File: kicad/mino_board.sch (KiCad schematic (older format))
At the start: 40 parts, among them J1-2 Conn_01x04, J10 Conn_01x04, J2 Conn_01x05, J4 Conn_02x10_Counter_Clockwise, P1 LED, P2 LED, P3 LED, P4 LED, X1 SW_Push, Y1 SW_Push

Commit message: More footprints again
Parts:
- added JEXTRAS: Conn_01x05, symbol Connector_Generic:Conn_01x05
- added JPS5JUMPER: Conn_01x02, symbol Connector_Generic:Conn_01x02
- added SW_THUMBR: SW_SPDT, symbol Switch:SW_SPDT
- renumbered SW_THUMBS to SW_THUMBL
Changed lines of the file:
@@
 $EndComp
 $Comp
-L Switch:SW_SPDT SW_THUMBS
+L Switch:SW_SPDT SW_THUMBL
 U 1 1 61698E4A
 P 5550 950
-F 0 "SW_THUMBS" H 5550 1235 50  0000 C CNN
+F 0 "SW_THUMBL" H 5550 1235 50  0000 C CNN
 F 1 "SW_SPDT" H 5550 1144 50  0000 C CNN
 F 2 "" H 5550 950 50  0001 C CNN
@@
 	1    0    0    -1
 $EndComp
+$Comp
+L Switch:SW_SPDT SW_THUMBR
+U 1 1 6169939A
+P 5550 1650
+F 0 "SW_THUMBR" H 5550 1935 50  0000 C CNN
+F 1 "SW_SPDT" H 5550 1844 50  0000 C CNN
+F 2 "" H 5550 1650 50  0001 C CNN
+F 3 "~" H 5550 1650 50  0001 C CNN
+	1    5550 1650
+	1    0    0    -1
+$EndComp
+$Comp
+L Connector_Generic:Conn_01x05 JEXTRAS
+U 1 1 616AC5C6
+P 9650 1250
+F 0 "JEXTRAS" H 9730 1292 50  0000 L CNN
+F 1 "Conn_01x05" H 9730 1201 50  0000 L CNN
+F 2 "" H 9650 1250 50  0001 C CNN
+F 3 "~" H 9650 1250 50  0001 C CNN
+	1    9650 1250
+	1    0    0    -1
+$EndComp
+$Comp
+L Connector_Generic:Conn_01x02 JPS5JUMPER
+U 1 1 616B1ABF
+P 9450 2300
+F 0 "JPS5JUMPER" H 9530 2292 50  0000 L CNN
+F 1 "Conn_01x02" H 9530 2201 50  0000 L CNN
+F 2 "" H 9450 2300 50  0001 C CNN
+F 3 "~" H 9450 2300 50  0001 C CNN
+	1    9450 2300
+	1    0    0    -1
+$EndComp

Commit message: WIring and changes
Wire everything except audio, remove the PS5 board bits temporarily until I become more familiar with how it works.
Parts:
- removed JEXTRAS: Conn_01x05, symbol Connector_Generic:Conn_01x05
- removed JPS51: Conn_01x06, symbol Connector_Generic:Conn_01x06
- removed JPS52, JPS5JUMPER: Conn_01x02, symbol Connector_Generic:Conn_01x02
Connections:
- net at J4.3 (Pin_3), RIGHT1.1: now also SW_THUMBR.1 (A); no longer RIGHT2.1
- net at J4.4 (Pin_4), LEFT1.1: now also SW_THUMBL.1 (A); no longer LEFT2.1
- net at J10.2 (Pin_2), L3.1: now also SW_THUMBL.3 (C)
- net at J10.3 (Pin_3), R3.1: now also SW_THUMBR.3 (C)
- net at SW_SOCD.1 (A): now also JSOCD.1 (Pin_1)
- net at SW_SOCD.2 (B): now also JSOCD.2 (Pin_2)
- net at SW_THUMBL.2 (B): now also LEFT2.1
- net at SW_THUMBR.2 (B): now also RIGHT2.1
- net at SW_STICK.1: now also JSTICKTYPE.1 (Pin_1)
- net at SW_STICK.2: now also JSTICKTYPE.3 (Pin_3)
- net at SW_STICK.3: now also JSTICKTYPE.2 (Pin_2)
- net at SW_STICK.4: now also JSTICKTYPE.4 (Pin_4)
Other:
- moved on the sheet: JAUDIO, JSOCD, JSTICKTYPE, SW_THUMBL, SW_THUMBR
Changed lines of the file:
@@
 	4300 7600 5550 7600
 Wire Wire Line
-	5550 7600 5550 4850
-Wire Wire Line
-	5550 4850 5650 4850
-Wire Wire Line
-	5550 4850 5550 4350
-Wire Wire Line
 	5550 4350 5650 4350
-Connection ~ 5550 4850
 Wire Wire Line
 	3850 5350 4100 5350
@@
 	4100 7400 1750 7400
 Wire Wire Line
-	1750 7400 1750 6400
-Wire Wire Line
-	1750 6400 1950 6400
-Wire Wire Line
-	1750 6400 1750 5950
-Wire Wire Line
 	1750 5950 1950 5950
-Connection ~ 1750 6400
 Wire Wire Line
 	3850 5250 4400 5250
@@
 	9700 5800 7450 5800
 Wire Wire Line
-	7450 5800 7450 5950
+	7450 5800 7450 5900
 Wire Wire Line
 	9700 5900 8100 5900
 Wire Wire Line
-	8100 5900 8100 5600
+	8100 5900 8100 5650
 $Comp
 L Switch:SW_SPDT SW_SOCD
@@
 $EndComp
 $Comp
-L Switch:SW_SPDT SW_THUMBL
-U 1 1 61698E4A
-P 5550 950
-F 0 "SW_THUMBL" H 5550 1235 50  0000 C CNN
-F 1 "SW_SPDT" H 5550 1144 50  0000 C CNN
-F 2 "" H 5550 950 50  0001 C CNN
-F 3 "~" H 5550 950 50  0001 C CNN
-	1    5550 950
-	1    0    0    -1
-$EndComp
-$Comp
 L Switch:SW_SP3T SW_STICK
 U 1 1 6169A4AE
@@
 L Connector_Generic:Conn_01x04 JSTICKTYPE
 U 1 1 616A468F
-P 7700 2350
-F 0 "JSTICKTYPE" H 7780 2342 50  0000 L CNN
-F 1 "Conn_01x04" H 7780 2251 50  0000 L CNN
-F 2 "" H 7700 2350 50  0001 C CNN
-F 3 "~" H 7700 2350 50  0001 C CNN
-	1    7700 2350
-	1    0    0    -1
-$EndComp
-$Comp
-L Connector_Generic:Conn_01x02 JPS52
-U 1 1 616A5060
-P 7650 3000
-F 0 "JPS52" H 7730 2992 50  0000 L CNN
-F 1 "Conn_01x02" H 7730 2901 50  0000 L CNN
-F 2 "" H 7650 3000 50  0001 C CNN
-F 3 "~" H 7650 3000 50  0001 C CNN
-	1    7650 3000
+P 6900 1550
+F 0 "JSTICKTYPE" H 6980 1542 50  0000 L CNN
+F 1 "Conn_01x04" H 6980 1451 50  0000 L CNN
+F 2 "" H 6900 1550 50  0001 C CNN
+F 3 "~" H 6900 1550 50  0001 C CNN
+	1    6900 1550
 	1    0    0    -1
 $EndComp
@@
 L Connector_Generic:Conn_01x02 JSOCD
 U 1 1 616A5F1B
-P 7650 3450
-F 0 "JSOCD" H 7730 3442 50  0000 L CNN
-F 1 "Conn_01x02" H 7730 3351 50  0000 L CNN
-F 2 "" H 7650 3450 50  0001 C CNN
-F 3 "~" H 7650 3450 50  0001 C CNN
-	1    7650 3450
-	1    0    0    -1
-$EndComp
-$Comp
-L Connector_Generic:Conn_01x06 JPS51
-U 1 1 616A6B41
-P 9000 3200
-F 0 "JPS51" H 9080 3192 50  0000 L CNN
-F 1 "Conn_01x06" H 9080 3101 50  0000 L CNN
-F 2 "" H 9000 3200 50  0001 C CNN
-F 3 "~" H 9000 3200 50  0001 C CNN
-	1    9000 3200
+P 5050 950
+F 0 "JSOCD" H 5130 942 50  0000 L CNN
+F 1 "Conn_01x02" H 5130 851 50  0000 L CNN
+F 2 "" H 5050 950 50  0001 C CNN
+F 3 "~" H 5050 950 50  0001 C CNN
+	1    5050 950
 	1    0    0    -1
 $EndComp
@@
 L Connector_Generic:Conn_01x06 JAUDIO
 U 1 1 616A715C
-P 9000 4000
-F 0 "JAUDIO" H 9080 3992 50  0000 L CNN
-F 1 "Conn_01x06" H 9080 3901 50  0000 L CNN
-F 2 "" H 9000 4000 50  0001 C CNN
-F 3 "~" H 9000 4000 50  0001 C CNN
-	1    9000 4000
+P 8800 1200
+F 0 "JAUDIO" H 8880 1192 50  0000 L CNN
+F 1 "Conn_01x06" H 8880 1101 50  0000 L CNN
+F 2 "" H 8800 1200 50  0001 C CNN
+F 3 "~" H 8800 1200 50  0001 C CNN
+	1    8800 1200
 	1    0    0    -1
 $EndComp
@@
 L Switch:SW_SPDT SW_THUMBR
 U 1 1 6169939A
-P 5550 1650
-F 0 "SW_THUMBR" H 5550 1935 50  0000 C CNN
-F 1 "SW_SPDT" H 5550 1844 50  0000 C CNN
-F 2 "" H 5550 1650 50  0001 C CNN
-F 3 "~" H 5550 1650 50  0001 C CNN
-	1    5550 1650
-	1    0    0    -1
-$EndComp
-$Comp
-L Connector_Generic:Conn_01x05 JEXTRAS
-U 1 1 616AC5C6
-P 9650 1250
-F 0 "JEXTRAS" H 9730 1292 50  0000 L CNN
-F 1 "Conn_01x05" H 9730 1201 50  0000 L CNN
-F 2 "" H 9650 1250 50  0001 C CNN
-F 3 "~" H 9650 1250 50  0001 C CNN
-	1    9650 1250
-	1    0    0    -1
-$EndComp
-$Comp
-L Connector_Generic:Conn_01x02 JPS5JUMPER
-U 1 1 616B1ABF
-P 9450 2300
-F 0 "JPS5JUMPER" H 9530 2292 50  0000 L CNN
-F 1 "Conn_01x02" H 9530 2201 50  0000 L CNN
-F 2 "" H 9450 2300 50  0001 C CNN
-F 3 "~" H 9450 2300 50  0001 C CNN
-	1    9450 2300
-	1    0    0    -1
-$EndComp
+P 6150 7150
+F 0 "SW_THUMBR" H 6150 7435 50  0000 C CNN
+F 1 "SW_SPDT" H 6150 7344 50  0000 C CNN
+F 2 "" H 6150 7150 50  0001 C CNN
+F 3 "~" H 6150 7150 50  0001 C CNN
+	1    6150 7150
+	-1   0    0    1
+$EndComp
+Wire Wire Line
+	5550 4350 5550 7250
+Wire Wire Line
+	1750 5950 1750 6950
+$Comp
+L Switch:SW_SPDT SW_THUMBL
+U 1 1 61698E4A
+P 1300 6400
+F 0 "SW_THUMBL" H 1300 6685 50  0000 C CNN
+F 1 "SW_SPDT" H 1300 6594 50  0000 C CNN
+F 2 "" H 1300 6400 50  0001 C CNN
+F 3 "~" H 1300 6400 50  0001 C CNN
+	1    1300 6400
+	-1   0    0    1
+$EndComp
+Wire Wire Line
+	5550 7250 5950 7250
+Connection ~ 5550 7250
+Wire Wire Line
+	5550 7250 5550 7600
+Wire Wire Line
+	6350 7150 6350 6450
+Wire Wire Line
+	6350 6450 5400 6450
+Wire Wire Line
+	5400 6450 5400 4850
+Wire Wire Line
+	5400 4850 5650 4850
+Wire Wire Line
+	1500 6400 1950 6400
+Wire Wire Line
+	1750 6950 800  6950
+Wire Wire Line
+	800  6950 800  6500
+Wire Wire Line
+	800  6500 1100 6500
+Connection ~ 1750 6950
+Wire Wire Line
+	1750 6950 1750 7400
+Wire Wire Line
+	7450 5900 6500 5900
+Wire Wire Line
+	6500 5900 6500 7750
+Wire Wire Line
+	6500 7750 550  7750
+Wire Wire Line
+	550  7750 550  6300
+Wire Wire Line
+	550  6300 1100 6300
+Connection ~ 7450 5900
+Wire Wire Line
+	7450 5900 7450 5950
+Wire Wire Line
+	8100 5650 6150 5650
+Wire Wire Line
+	6150 5650 6150 6900
+Wire Wire Line
+	6150 6900 5800 6900
+Wire Wire Line
+	5800 6900 5800 7050
+Wire Wire Line
+	5800 7050 5950 7050
+Connection ~ 8100 5650
+Wire Wire Line
+	8100 5650 8100 5600
+Wire Wire Line
+	4850 950  4850 850
+Wire Wire Line
+	4850 850  4650 850
+Wire Wire Line
+	4850 1050 4850 1300
+Wire Wire Line
+	4850 1300 3900 1300
+Wire Wire Line
+	3900 1300 3900 950
+Wire Wire Line
+	3900 950  4250 950
+Wire Wire Line
+	6700 1550 6500 1550
+Wire Wire Line
+	6500 1550 6500 950
+Wire Wire Line
+	6900 950  7300 950
+Wire Wire Line
+	7300 950  7300 2100
+Wire Wire Line
+	7300 2100 6400 2100
+Wire Wire Line
+	6400 2100 6400 1650
+Wire Wire Line
+	6400 1650 6700 1650
+Wire Wire Line
+	6900 850  7100 850
+Wire Wire Line
+	7100 850  7100 1200
+Wire Wire Line
+	7100 1200 6600 1200
+Wire Wire Line
+	6600 1200 6600 1450
+Wire Wire Line
+	6600 1450 6700 1450
+Wire Wire Line
+	6900 1050 7500 1050
+Wire Wire Line
+	7500 1050 7500 1950
+Wire Wire Line
+	7500 1950 6700 1950
+Wire Wire Line
+	6700 1950 6700 1750
 $EndSCHEMATC

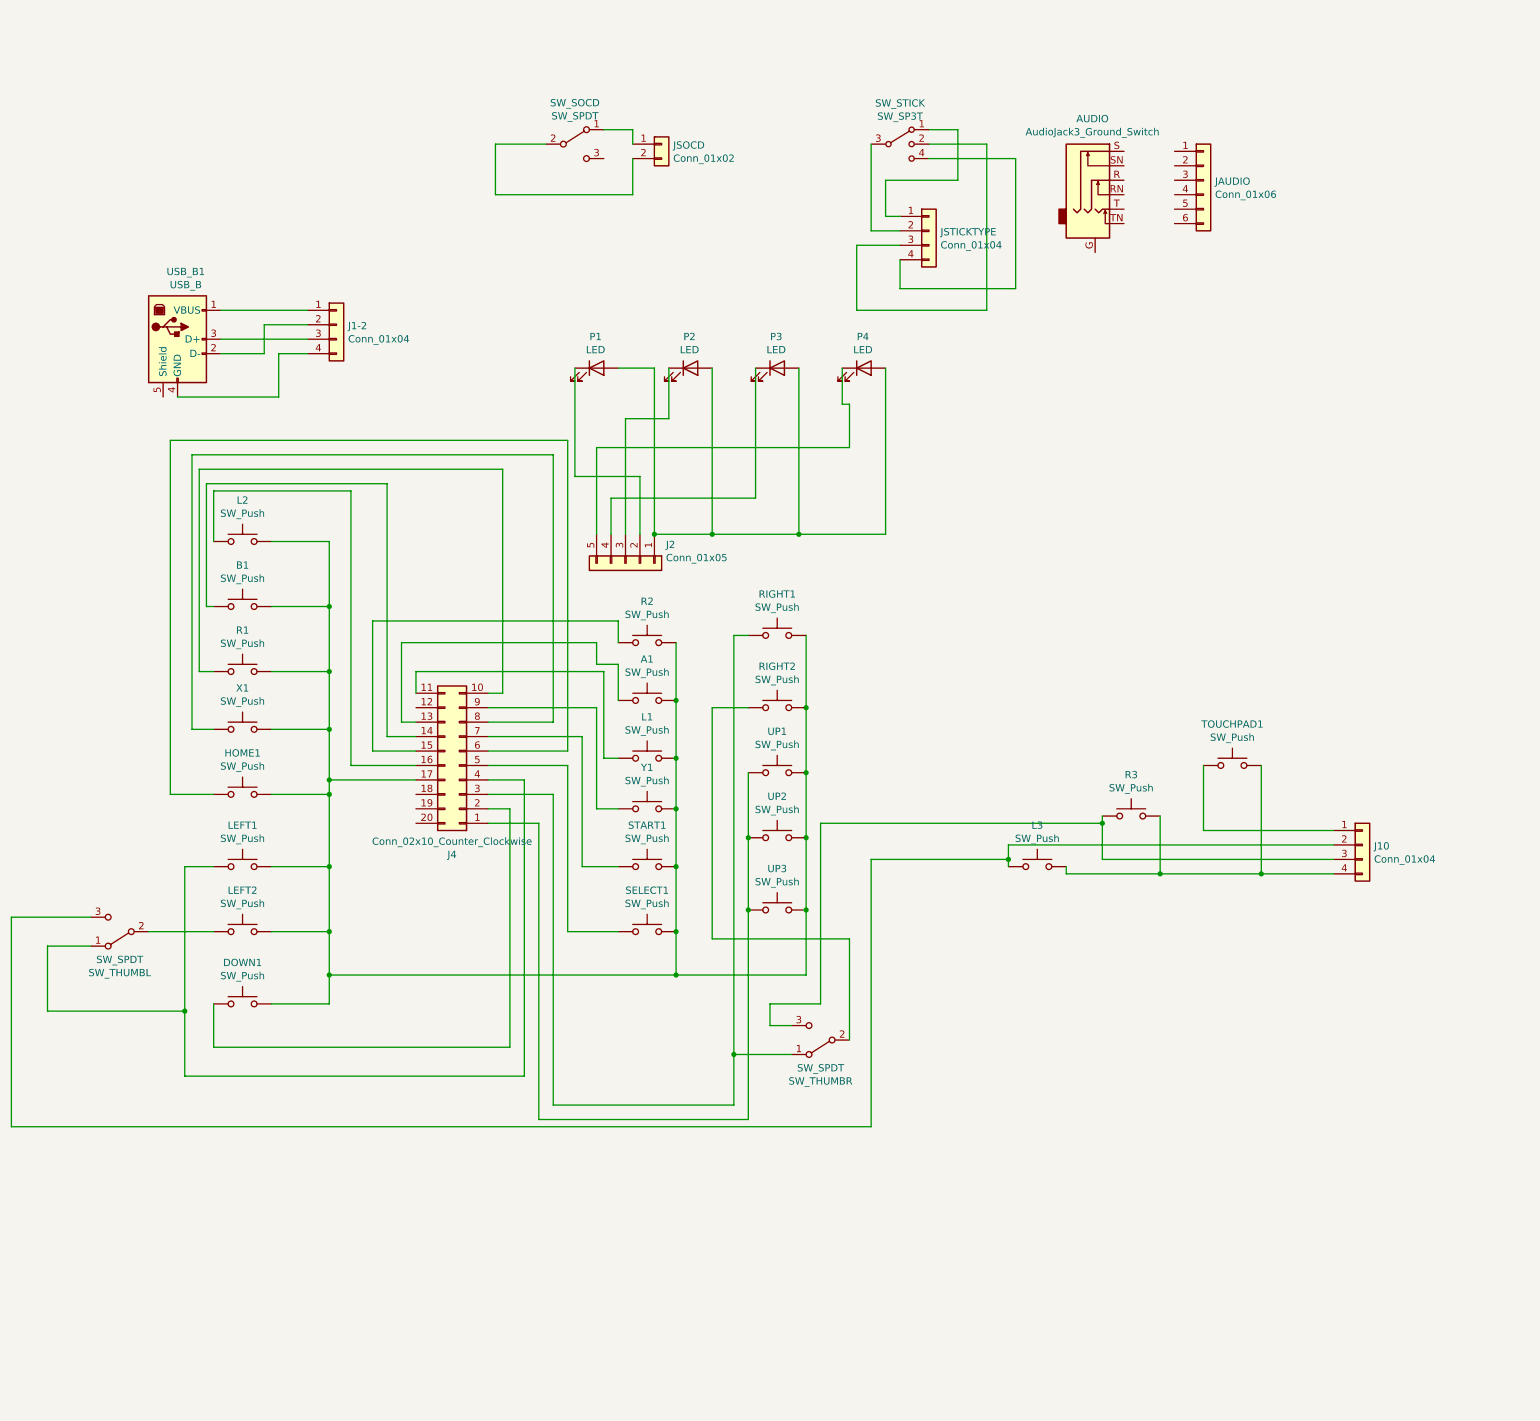
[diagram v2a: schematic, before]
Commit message: Dip Switches
Swap out the toggle switches for dip switches to control the spare thumb buttons.
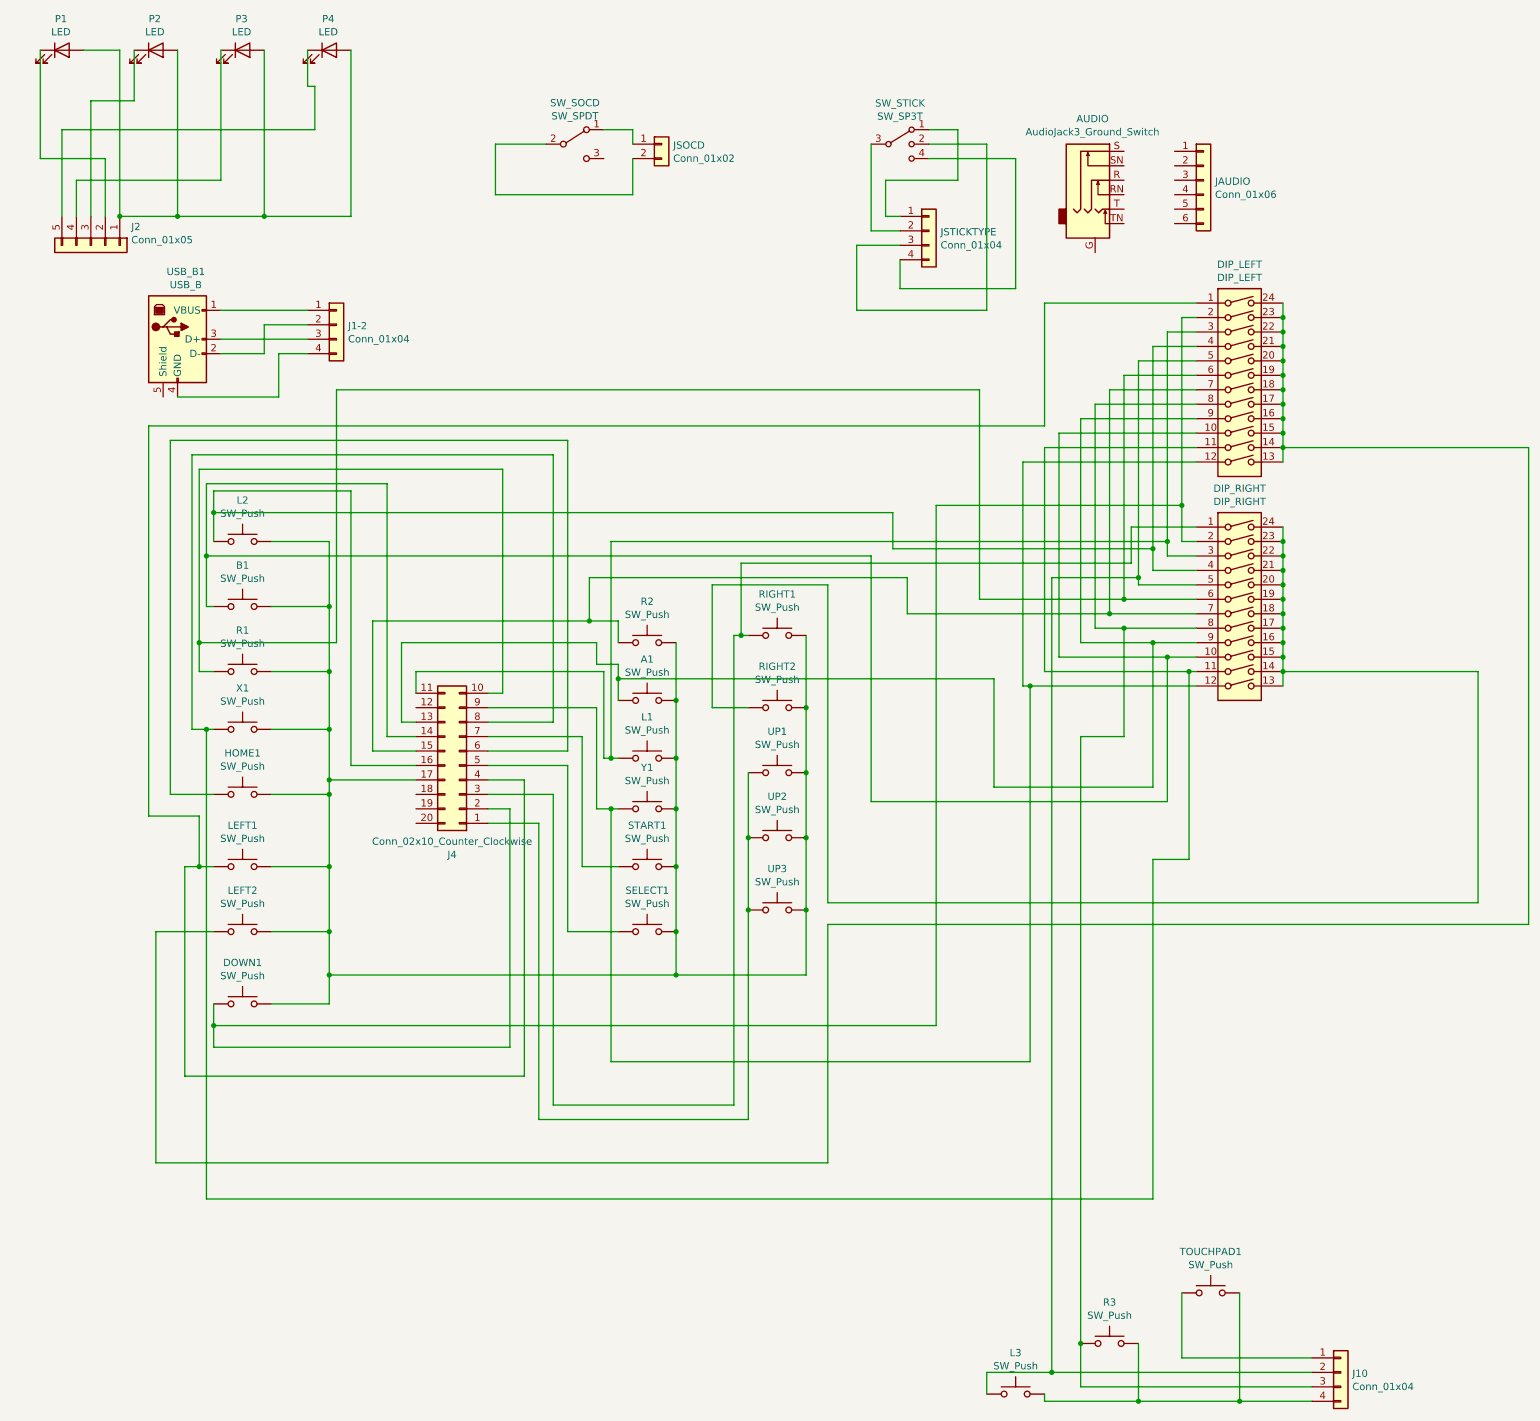
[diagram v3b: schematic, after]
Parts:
- removed SW_THUMBL, SW_THUMBR: SW_SPDT, symbol Switch:SW_SPDT
- added DIP_LEFT: DIP_LEFT, symbol Switch:SW_DIP_x12
- added DIP_RIGHT: DIP_RIGHT, symbol Switch:SW_DIP_x12
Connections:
- net at J4.10 (Pin_10), R1.1: now also DIP_LEFT.6, DIP_RIGHT.6
- net at J4.11 (Pin_11), L1.1: now also DIP_LEFT.3, DIP_RIGHT.3
- net at A1.1, J4.13 (Pin_13): now also DIP_LEFT.9, DIP_RIGHT.9
- net at B1.1, J4.14 (Pin_14): now also DIP_LEFT.10, DIP_RIGHT.10
- net at J4.15 (Pin_15), R2.1: now also DIP_LEFT.7, DIP_RIGHT.7
- net at J4.16 (Pin_16), L2.1: now also DIP_LEFT.4, DIP_RIGHT.4
- net at DOWN1.1, J4.2 (Pin_2): now also DIP_LEFT.2, DIP_RIGHT.2
- net at J4.3 (Pin_3), RIGHT1.1: now also DIP_RIGHT.1
- net at J4.4 (Pin_4), LEFT1.1: now also DIP_LEFT.1
- net at J4.8 (Pin_8), X1.1: now also DIP_LEFT.11, DIP_RIGHT.11
- net at J4.9 (Pin_9), Y1.1: now also DIP_LEFT.12, DIP_RIGHT.12
- net at J10.2 (Pin_2), L3.1: now also DIP_LEFT.5, DIP_RIGHT.5
- net at J10.3 (Pin_3), R3.1: now also DIP_LEFT.8, DIP_RIGHT.8
- net at RIGHT2.1: now also DIP_RIGHT.13, DIP_RIGHT.14, DIP_RIGHT.15, DIP_RIGHT.16, DIP_RIGHT.17, DIP_RIGHT.18, DIP_RIGHT.19, DIP_RIGHT.20, DIP_RIGHT.21, DIP_RIGHT.22, DIP_RIGHT.23, DIP_RIGHT.24
- net at LEFT2.1: now also DIP_LEFT.13, DIP_LEFT.14, DIP_LEFT.15, DIP_LEFT.16, DIP_LEFT.17, DIP_LEFT.18, DIP_LEFT.19, DIP_LEFT.20, DIP_LEFT.21, DIP_LEFT.22, DIP_LEFT.23, DIP_LEFT.24
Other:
- moved on the sheet: J10, J2, L3, P1, P2, P3, P4, R3, TOUCHPAD1

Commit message: Remove Audio Jack
Remove the audio jack until I can figure out how it works
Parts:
- removed AUDIO: AudioJack3_Ground_Switch, symbol Connector:AudioJack3_Ground_Switch
- removed JAUDIO: Conn_01x06, symbol Connector_Generic:Conn_01x06
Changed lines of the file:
@@
-$EndComp
-$Comp
-L Connector:AudioJack3_Ground_Switch AUDIO
-U 1 1 616A2FE6
-P 8050 1200
-F 0 "AUDIO" H 8032 1625 50  0000 C CNN
-F 1 "AudioJack3_Ground_Switch" H 8032 1534 50  0000 C CNN
-F 2 "" H 8050 1200 50  0001 C CNN
-F 3 "~" H 8050 1200 50  0001 C CNN
-	1    8050 1200
-	1    0    0    -1
 $EndComp
 $Comp
@@
 	1    0    0    -1
 $EndComp
-$Comp
-L Connector_Generic:Conn_01x06 JAUDIO
-U 1 1 616A715C
-P 8800 1200
-F 0 "JAUDIO" H 8880 1192 50  0000 L CNN
-F 1 "Conn_01x06" H 8880 1101 50  0000 L CNN
-F 2 "" H 8800 1200 50  0001 C CNN
-F 3 "~" H 8800 1200 50  0001 C CNN
-	1    8800 1200
-	1    0    0    -1
-$EndComp

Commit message: Route the new board
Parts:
- renumbered DIP_LEFT to DIP_LEFT1, DIP_RIGHT to DIP_RIGHT1, JSOCD to JSOCD1, JSTICKTYPE to JSTICKTYPE1, SW_SOCD to SW_SOCD1, SW_STICK to SW_STICK1
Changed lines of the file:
@@
 	9550 9550 7950 9550
 $Comp
-L Switch:SW_SPDT SW_SOCD
+L Switch:SW_SPDT SW_SOCD1
 U 1 1 61698368
 P 4450 950
-F 0 "SW_SOCD" H 4450 1235 50  0000 C CNN
+F 0 "SW_SOCD1" H 4450 1235 50  0000 C CNN
 F 1 "SW_SPDT" H 4450 1144 50  0000 C CNN
 F 2 "" H 4450 950 50  0001 C CNN
@@
 $EndComp
 $Comp
-L Switch:SW_SP3T SW_STICK
+L Switch:SW_SP3T SW_STICK1
 U 1 1 6169A4AE
 P 6700 950
-F 0 "SW_STICK" H 6700 1233 50  0000 C CNN
+F 0 "SW_STICK1" H 6700 1233 50  0000 C CNN
 F 1 "SW_SP3T" H 6700 1142 50  0000 C CNN
 F 2 "" H 6075 1125 50  0001 C CNN
@@
 $EndComp
 $Comp
-L Connector_Generic:Conn_01x04 JSTICKTYPE
+L Connector_Generic:Conn_01x04 JSTICKTYPE1
 U 1 1 616A468F
 P 6900 1550
-F 0 "JSTICKTYPE" H 6980 1542 50  0000 L CNN
+F 0 "JSTICKTYPE1" H 6980 1542 50  0000 L CNN
 F 1 "Conn_01x04" H 6980 1451 50  0000 L CNN
 F 2 "" H 6900 1550 50  0001 C CNN
@@
 $EndComp
 $Comp
-L Connector_Generic:Conn_01x02 JSOCD
+L Connector_Generic:Conn_01x02 JSOCD1
 U 1 1 616A5F1B
 P 5050 950
-F 0 "JSOCD" H 5130 942 50  0000 L CNN
+F 0 "JSOCD1" H 5130 942 50  0000 L CNN
 F 1 "Conn_01x02" H 5130 851 50  0000 L CNN
 F 2 "" H 5050 950 50  0001 C CNN
@@
 	5550 4350 5550 7600
 $Comp
-L Switch:SW_DIP_x12 DIP_RIGHT
+L Switch:SW_DIP_x12 DIP_RIGHT1
 U 1 1 616F6512
 P 9050 4200
-F 0 "DIP_RIGHT" H 9050 5067 50  0000 C CNN
+F 0 "DIP_RIGHT1" H 9050 5067 50  0000 C CNN
 F 1 "DIP_RIGHT" H 9050 4976 50  0000 C CNN
 F 2 "" H 9050 4200 50  0001 C CNN
@@
 $EndComp
 $Comp
-L Switch:SW_DIP_x12 DIP_LEFT
+L Switch:SW_DIP_x12 DIP_LEFT1
 U 1 1 616F93A3
 P 9050 2650
-F 0 "DIP_LEFT" H 9050 3517 50  0000 C CNN
+F 0 "DIP_LEFT1" H 9050 3517 50  0000 C CNN
 F 1 "DIP_LEFT" H 9050 3426 50  0000 C CNN
 F 2 "" H 9050 2650 50  0001 C CNN
